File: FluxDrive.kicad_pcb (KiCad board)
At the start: 2 copper layers, 60 x 48 mm, 124 parts, among them J1 Amiga floppy 34, J2 Floppy power, J3 USB-C, J4 UART / recovery, J5 Spare GPIO, SW1 BOOT, SW2 RESET, U1 ESP32-S3-WROOM-1-N16R8, U2 74LVC14A, U3 74LVC14A, U4 74LVC07A, U5 TPS259531, U6 TLV62569DBVR, U7 USBLC6-2SC6

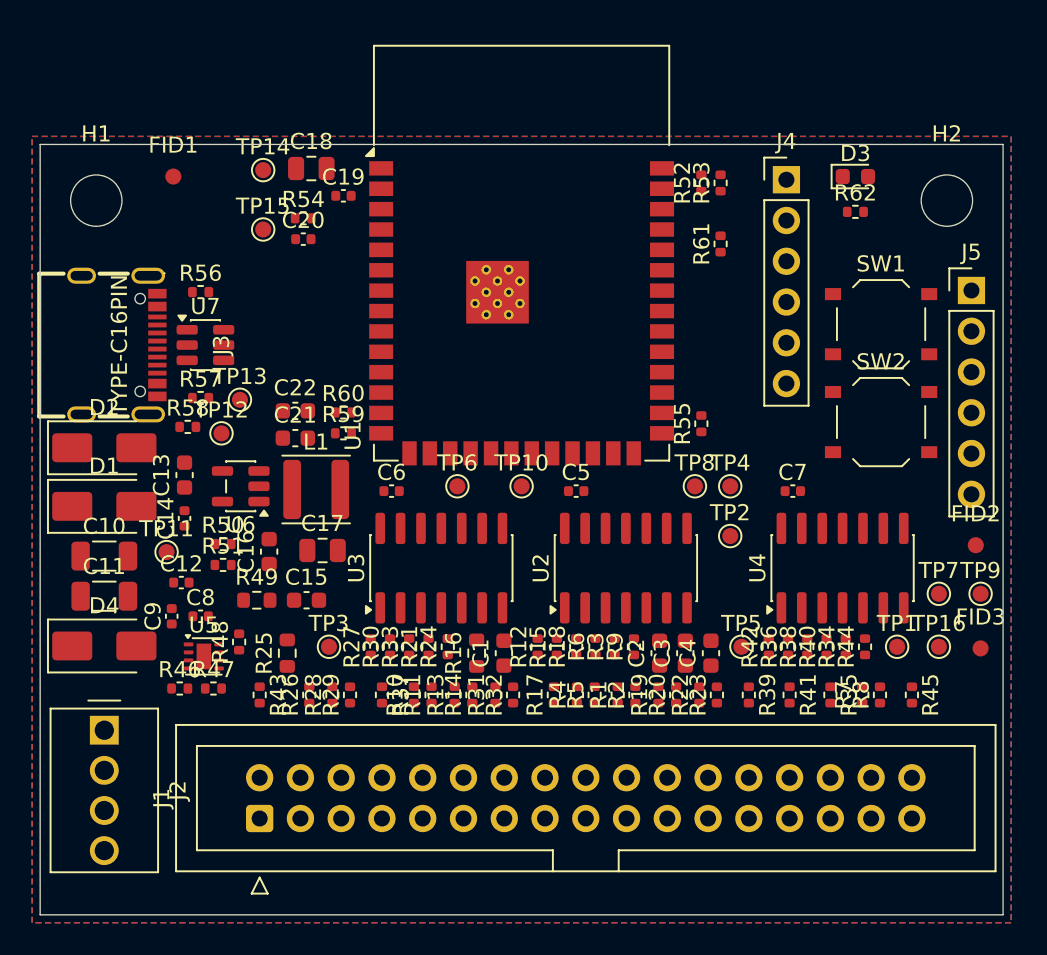
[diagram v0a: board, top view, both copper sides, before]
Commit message: Board: routed, DRC clean
- tools/pcb_build.sh builds the board in build/pcb (OUT= to choose): netlist, sync, placement,
  hand-made USB-C VBUS bridge, GND fan-out, Freerouting x6 in parallel with the best kept,
  finishing (maze, Freerouting --continue), loose ends, ground stitching, silkscreen, DRC
- routing tools from the Nano-Tek, for 2 layers: GND stays plane (no pins in the DSN),
  B.Cu four times as dear as F.Cu, track keep-out on B.Cu between the J1 pin rows
- placement: buffers higher, row B at 1.3 mm pitch, room for the rails between the rows,
  spare header east of U4, connector test pads south of J1
- DRC: 0 errors, 0 unconnected, 0 parity issues; buck 32 mm from /DKRD, 21 mm from the antenna
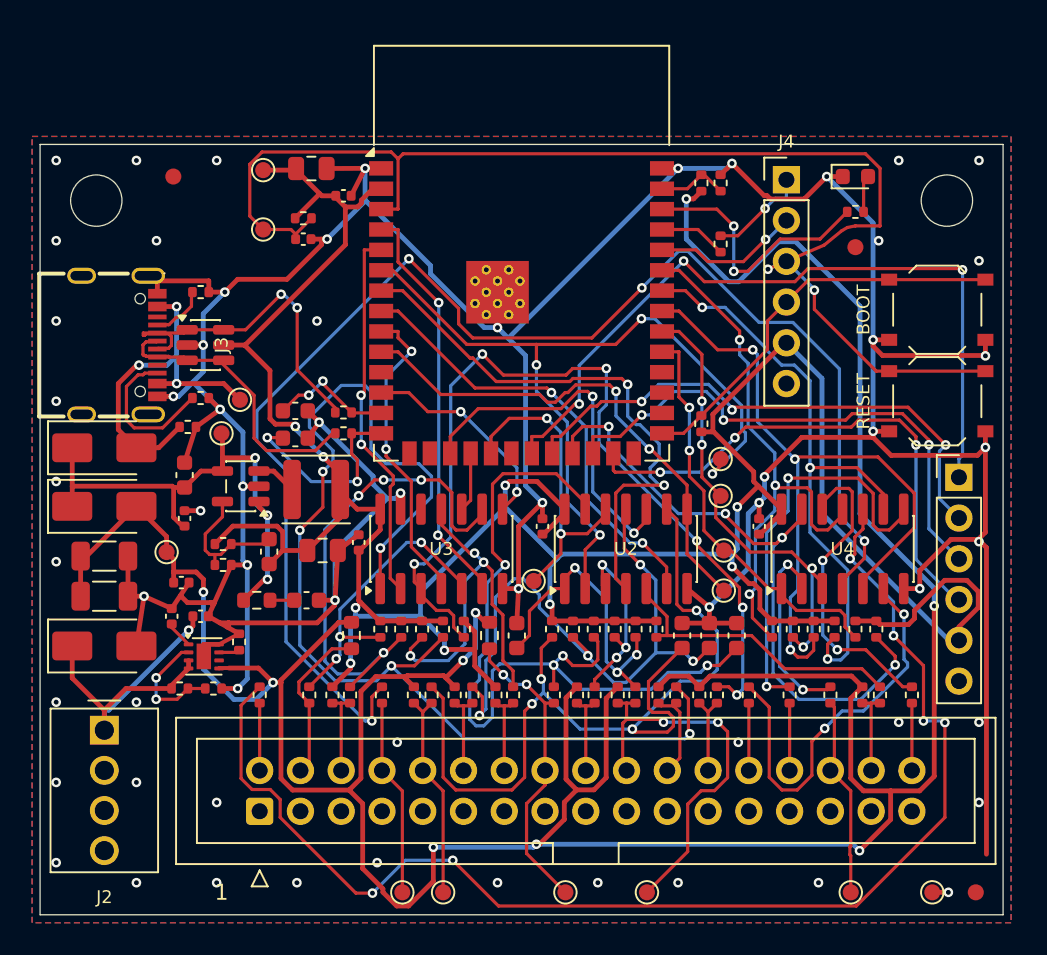
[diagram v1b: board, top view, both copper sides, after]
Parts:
- moved TP9 31.9 mm to (132.7, 146.6)
- moved TP7 26.0 mm to (137.8, 146.6)
- moved TP5 24.1 mm to (125.1, 146.6)
- moved FID2 20.0 mm to (150.8, 106.4)
- moved TP6 17.8 mm to (142.6, 127.8)
- moved TP3 16.0 mm to (122.6, 146.6)
- moved TP1 15.6 mm to (150.5, 146.6)
- moved TP16 15.3 mm to (155.6, 146.6)
- moved FID3 15.2 mm to (158.3, 146.6)
- moved J5 11.7 mm to (157.2, 120.7)
- moved TP10 5.95 mm to (130.8, 127.2)
- moved R25 4.15 mm to (119.4, 130.6)
- moved C6 3.80 mm to (119.8, 124.8), turned to 90 degrees
- moved SW2 3.73 mm to (155.9, 116.0)
- moved SW1 3.61 mm to (155.9, 110.3)
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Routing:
- net /GND: track 0.00 -> 278.9 mm, vias 0 -> 63
- net /+5V_A: track 0.00 -> 206.4 mm, vias 0 -> 9
- net /+3V3: track 0.00 -> 194.8 mm, vias 0 -> 9
- net /INDEX_D: track 0.00 -> 87.9 mm, vias 0 -> 4
- net /ESP_EN: track 0.00 -> 81.9 mm, vias 0 -> 2
- net /CHNG_D: track 0.00 -> 80.7 mm, vias 0 -> 6
- net /DKWD_B: track 0.00 -> 71.7 mm, vias 0 -> 5
- net /SEL0_B: track 0.00 -> 56.1 mm, vias 0 -> 4
- net /DKWE_B: track 0.00 -> 55.8 mm, vias 0 -> 6
- net /MTR0_B: track 0.00 -> 51.2 mm, vias 0 -> 4
- net /STEP: track 0.00 -> 50.9 mm, vias 0 -> 4
- net /GPIO13: track 0.00 -> 47.8 mm, vias 0 -> 3
- net /TRK0_N: track 0.00 -> 45.0 mm, vias 0 -> 3
- net /RDY_N: track 0.00 -> 40.6 mm, vias 0 -> 4
- net /SEL1_B: track 0.00 -> 39.6 mm, vias 0 -> 4
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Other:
- board text added: "+5V"
- board text added: "1"
- board text added: "12V nc"
- board text added: "3V3"
- board text added: "50 mm"
- board text added: "BOOT"
- board text added: "EN"
- board text added: "FluxDrive v1 rev A"
- board text added: "GND"
- board text added: "IO0"
- board text added: "IO13"
- board text added: "IO14"
- board text added: "IO47"
- board text added: "IO48"
- board text added: "J1 option: 2x17 FEMALE socket on this side, plugs straight"
- board text added: "JLCJLCJLCJLC"
- board text added: "RESET"
- board text added: "RX"
- board text added: "S/N"
- board text added: "TX"
- board text added: "UART"
- board text added: "by Dimmy (Dimitri Hilverda)"
- board text added: "onto the A500 floppy header. Pin 1 = square pad"

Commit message: Layout review and fixes: 4 layers, antenna on the board
Four specialist reviews of the task-10 layout (55 findings, 13 major); the
record with every decision is docs/reviews/2026-09-29-layout-review.md.

- 4 layers (Dimitri): In1 solid GND, In2 solid +3V3; every GND/+3V3 pad
  has its own via, outer pours stitched to In1.
- The board grows 6.5 mm north; the module's antenna lies 0.5 mm inside
  the edge over copper-free board (Dimitri; O10 closed). Spec v0.4.
- Buffer gates re-assigned in connector order (U3 pins 4-16, U2 18-32);
  row B follows the buffer inputs; schematic and PDF regenerated.
- Rule areas: J1 rows, antenna edge, buck, module underside, USB-C body.
- Hand routes before Freerouting: VBUS bridge, +5V_A rail, eFuse, USB
  D+/D- pad joins, /DKRD_D (6.4 mm, no via).
- Build scripts: deterministic fan-out, planes in the DSN, varied
  Freerouting runs, pads' own clearance in the stitching, placement check,
  fit template with scale bars, note and STEP.

Build 12: DRC 0 errors, 0 unconnected, 0 parity; 71 tests pass.
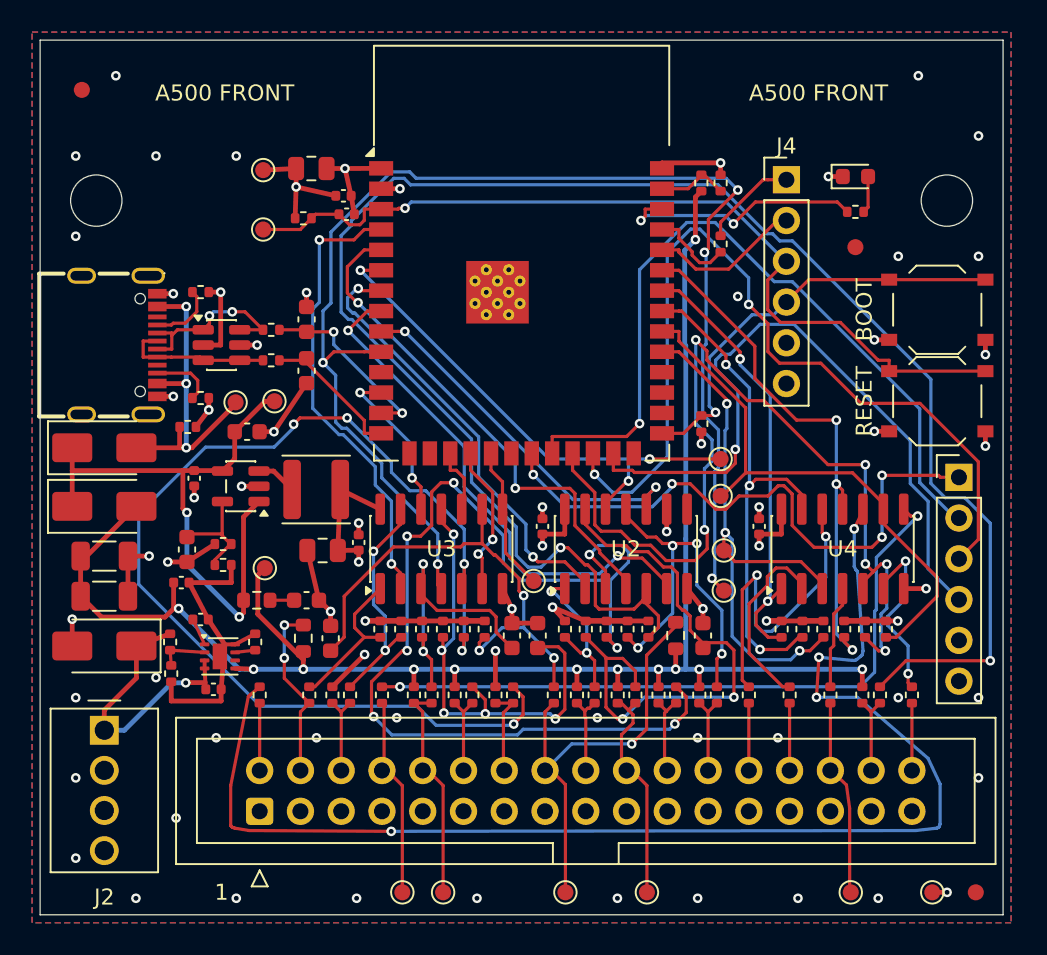
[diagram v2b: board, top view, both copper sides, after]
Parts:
- moved C4 25.3 mm to (118.1, 130.8)
- moved C1 11.6 mm to (141.3, 130.6)
- moved R16 11.6 mm to (139.6, 130.6), turned to -90 degrees
- moved C3 10.7 mm to (131.0, 130.6)
- moved C2 10.6 mm to (129.4, 130.6)
- moved R21 10.2 mm to (135.3, 130.2)
- moved R24 10.2 mm to (136.6, 130.2)
- moved R12 8.10 mm to (123.8, 130.2)
- moved R15 8.10 mm to (125.1, 130.2)
- moved FID1 7.85 mm to (102.6, 96.6)
- moved R60 6.84 mm to (114.4, 111.5)
- moved R18 6.80 mm to (127.7, 130.2)
- moved R59 6.40 mm to (114.4, 113.5)
- moved TP11 6.20 mm to (114.0, 126.4)
- moved R36 5.80 mm to (152.7, 130.2)
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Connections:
- U2 pad 1: /STEP_B -> /DIR_B
- U2 pad 10: /SEL1 -> /DKWE
- U2 pad 11: /SEL1_B -> /DKWE_B
- U2 pad 12: /MTR0 -> /STEP
- U2 pad 13: /MTR0_B -> /STEP_B
- U2 pad 2: /STEP -> /DIR
- U2 pad 3: /DIR_B -> /DKWD_B
- U2 pad 4: /DIR -> /DKWD
- U2 pad 8: /SEL0 -> unconnected-(U2-Pad8)
- U2 pad 9: /SEL0_B -> /GND
- U3 pad 1: /DKWD_B -> /MTR0_P4_B
- U3 pad 10: /PIN14 -> /SEL1
- U3 pad 11: /PIN14_B -> /SEL1_B
- U3 pad 12: unconnected-(U3-Pad12) -> /PIN6
- U3 pad 13: /GND -> /PIN6_B
- U3 pad 2: /DKWD -> /MTR0_P4
- U3 pad 3: /DKWE_B -> /SEL0_B
- U3 pad 4: /DKWE -> /SEL0
- U3 pad 5: /MTR0_P4_B -> /PIN14_B
- U3 pad 6: /MTR0_P4 -> /PIN14
- U3 pad 8: /PIN6 -> /MTR0
- U3 pad 9: /PIN6_B -> /MTR0_B
- U4 pad 1: /DKRD_N -> /WPROT_N
- U4 pad 12: /RDY_D -> /TRK0_D
- U4 pad 13: /RDY_N -> /TRK0_N
- U4 pad 2: /DKRD_D -> /WPROT_D
- U4 pad 3: /INDEX_N -> /DKRD_N
- U4 pad 4: /INDEX_D -> /DKRD_D
- U4 pad 5: /TRK0_N -> /RDY_N
- U4 pad 6: /TRK0_D -> /RDY_D
- U4 pad 8: /WPROT_D -> /INDEX_D
- U4 pad 9: /WPROT_N -> /INDEX_N
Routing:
- net /GND: track 278.9 -> 73.2 mm, vias 63 -> 58
- net /+3V3: track 194.8 -> 66.3 mm, vias 9 -> 14
- net /+5V_A: track 206.4 -> 108.4 mm, vias 9 -> 12
- net /SIDE_B: track 18.8 -> 111.0 mm, vias 0 -> 2
- net /SEL0: track 31.8 -> 83.8 mm, vias 2 -> 5
- net /PIN14_B: track 24.1 -> 70.5 mm, vias 3 -> 5
- net /INDEX_D: track 87.9 -> 43.0 mm, vias 4 -> 2
- net /SEL0_B: track 56.1 -> 18.3 mm, vias 4 -> 2
- net /DKWE_B: track 55.8 -> 23.6 mm, vias 6 -> 4
- net /ESP_EN: track 81.9 -> 54.8 mm, vias 2 -> 1
- net /GPIO47: track 33.3 -> 54.5 mm, vias 3 -> 2
- net /MTR0_B: track 51.2 -> 31.0 mm, vias 4 -> 3
- net /SEL1: track 22.6 -> 4.12 mm, vias 2 -> 0
- net /STEP: track 50.9 -> 32.4 mm, vias 4 -> 3
- net /PIN6_B: track 31.6 -> 14.3 mm, vias 4 -> 2
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- added copper zone on In2.Cu, net /+3V3
- added copper zone on In1.Cu, net /GND
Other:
- board size 60 x 48 mm -> 60 x 54.5 mm
- copper layers 2 -> 4
- board text added: "40 mm"
- board text added: "A500 FRONT"
- board text added: "J1 option: 2x17 female socket on this side,"
- board text added: "plugs onto the A500 header. Pin 1 = square pad"
- board text added: "print at 100 %: both bars must measure exactly 50 mm / 40 mm"
- board text removed: "J1 option: 2x17 FEMALE socket on this side, plugs straight"
- board text removed: "onto the A500 floppy header. Pin 1 = square pad"
